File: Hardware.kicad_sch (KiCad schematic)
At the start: 30 parts, among them J1 Conn_01x06_Socket, J5 Conn_01x05_Socket, Q1 BC849, Q2 BC849, SW1 SW_Push, SW3 SW_Push, U1 ESP32-WROOM-32, U7 AMS1117-3.3

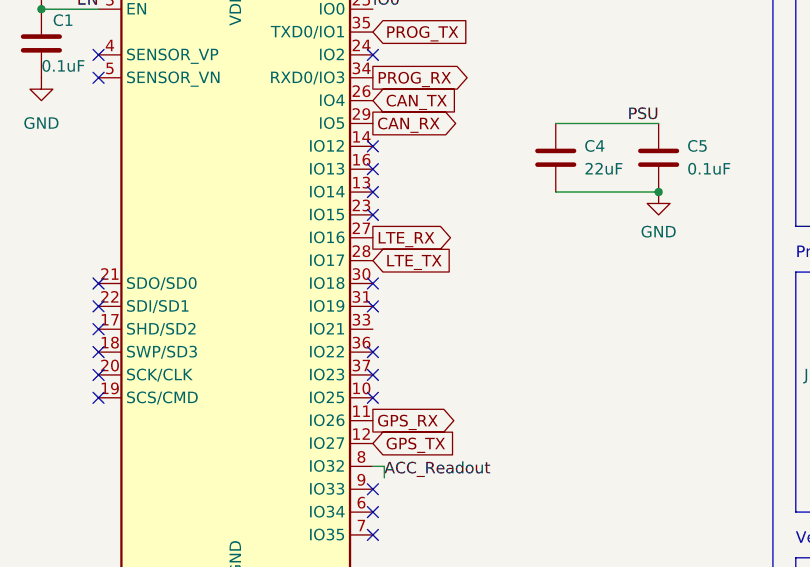
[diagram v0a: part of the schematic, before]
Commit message: updated schematics:
Fixed bug with PWKEY of LTE module

Fixed big with power
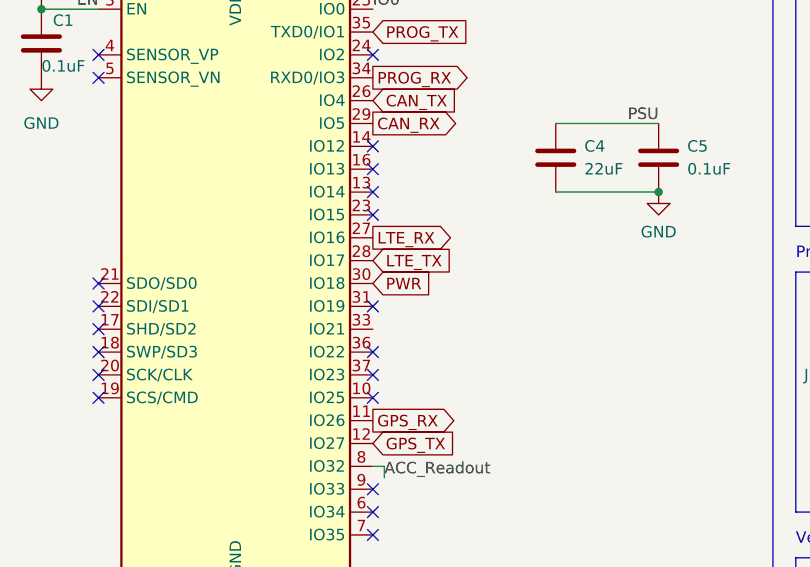
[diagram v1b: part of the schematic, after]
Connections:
- net PWR: now reaches U1.30 (IO18)
- no-connect marks 21 -> 20
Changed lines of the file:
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@@
-	)
-	(no_connect
-		(at 59.69 63.5)
 	)
 	(no_connect
@@
 			(effects
 				(font
+					(size 1.27 1.27)
+				)
+				(justify left)
+				(hide yes)
+			)
+		)
+	)
+	(global_label "PWR"
+		(shape input)
+		(at 59.69 63.5 0)
+		(fields_autoplaced yes)
+		(effects
+			(font
+				(size 1.27 1.27)
+			)
+			(justify left)
+		)
+		(property "Intersheetrefs" "${INTERSHEET_REFS}"
+			(at 66.6666 63.5 0)
+			(effects
+				(font

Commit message: first new layout
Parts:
- removed TP15, TP6: TestPoint, TestPoint:TestPoint_Pad_D1.5mm, symbol Connector:TestPoint
- C1, C22, C23, C5: value 0.1uF -> 100nF
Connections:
- net CAN_H: now also J5.4 (Pin_4); no longer J5.5 (Pin_5)
- net CAN_L: now also J5.5 (Pin_5); no longer J5.4 (Pin_4)
- net PSU renamed +3V3
